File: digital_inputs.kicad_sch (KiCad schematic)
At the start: 37 parts, among them U301 74HC595, U302 74HCT244

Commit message: completed schematic
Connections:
- net +3V3 renamed +3.3V

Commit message: placed components and began routing
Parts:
- RN301: footprint (none) -> Resistor_SMD:R_Array_Convex_8x0602
- U302: footprint Package_SO:SOIC-16_3.9x9.9mm_P1.27mm -> Package_SO:SOIC-20W_7.5x12.8mm_P1.27mm
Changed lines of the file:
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@@
       (effects (font (size 1.27 1.27)) (justify left))
     )
-    (property "Footprint" "Package_SO:SOIC-16_3.9x9.9mm_P1.27mm" (at 234.95 110.49 0)
+    (property "Footprint" "Package_SO:SOIC-20W_7.5x12.8mm_P1.27mm" (at 234.95 110.49 0)
       (effects (font (size 1.27 1.27)) hide)
     )
@@
       (effects (font (size 1.27 1.27)))
     )
-    (property "Footprint" "" (at 252.73 59.055 90)
-      (effects (font (size 1.27 1.27)) hide)
-    )
+    (property "Footprint" "Resistor_SMD:R_Array_Convex_8x0602" (at 252.73 59.055 90)
+      (effects (font (size 1.27 1.27)) hide)
+    )

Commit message: majority of layout done
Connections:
- net D_In_0_pullup: now also RN301.9 (R8.2); no longer RN301.16 (R1.2)
- net D_In_1_pullup: now also RN301.10 (R7.2); no longer RN301.15 (R2.2)
- net D_In_2_pullup: now also RN301.11 (R6.2); no longer RN301.14 (R3.2)
- net D_In_3_pullup: now also RN301.12 (R5.2); no longer RN301.13 (R4.2)
- net D_In_4_pullup: now also RN301.13 (R4.2); no longer RN301.12 (R5.2)
- net D_In_5_pullup: now also RN301.14 (R3.2); no longer RN301.11 (R6.2)
- net D_In_6_pullup: now also RN301.15 (R2.2); no longer RN301.10 (R7.2)
- net D_In_7_pullup: now also RN301.16 (R1.2); no longer RN301.9 (R8.2)
- net at RN301.1 (R1.1): now also U301.7 (QH); no longer U301.15 (QA)
- net at RN301.2 (R2.1): now also U301.6 (QG); no longer U301.1 (QB)
- net at RN301.3 (R3.1): now also U301.5 (QF); no longer U301.2 (QC)
- net at RN301.4 (R4.1): now also U301.4 (QE); no longer U301.3 (QD)
- net at RN301.5 (R5.1): now also U301.3 (QD); no longer U301.4 (QE)
- net at RN301.6 (R6.1): now also U301.2 (QC); no longer U301.5 (QF)
- net at RN301.7 (R7.1): now also U301.1 (QB); no longer U301.6 (QG)
- net at RN301.8 (R8.1): now also U301.15 (QA); no longer U301.7 (QH)
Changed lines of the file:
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@@
     )
   )
-  (symbol (lib_id "Device:R_Pack08") (at 252.73 46.99 270) (unit 1)
-    (in_bom yes) (on_board yes) (dnp no) (fields_autoplaced)
-    (property "Reference" "RN301" (at 252.73 30.48 90)
+  (symbol (lib_id "Device:R_Pack08") (at 252.73 44.45 270) (mirror x) (unit 1)
+    (in_bom yes) (on_board yes) (dnp no)
+    (property "Reference" "RN301" (at 252.73 60.96 90)
       (effects (font (size 1.27 1.27)))
     )
-    (property "Value" "10k" (at 252.73 33.02 90)
+    (property "Value" "10k" (at 252.73 58.42 90)
       (effects (font (size 1.27 1.27)))
     )
-    (property "Footprint" "Resistor_SMD:R_Array_Convex_8x0602" (at 252.73 59.055 90)
+    (property "Footprint" "Resistor_SMD:R_Array_Convex_8x0602" (at 252.73 32.385 90)
       (effects (font (size 1.27 1.27)) hide)
     )
-    (property "Datasheet" "~" (at 252.73 46.99 0)
+    (property "Datasheet" "~" (at 252.73 44.45 0)
       (effects (font (size 1.27 1.27)) hide)
     )

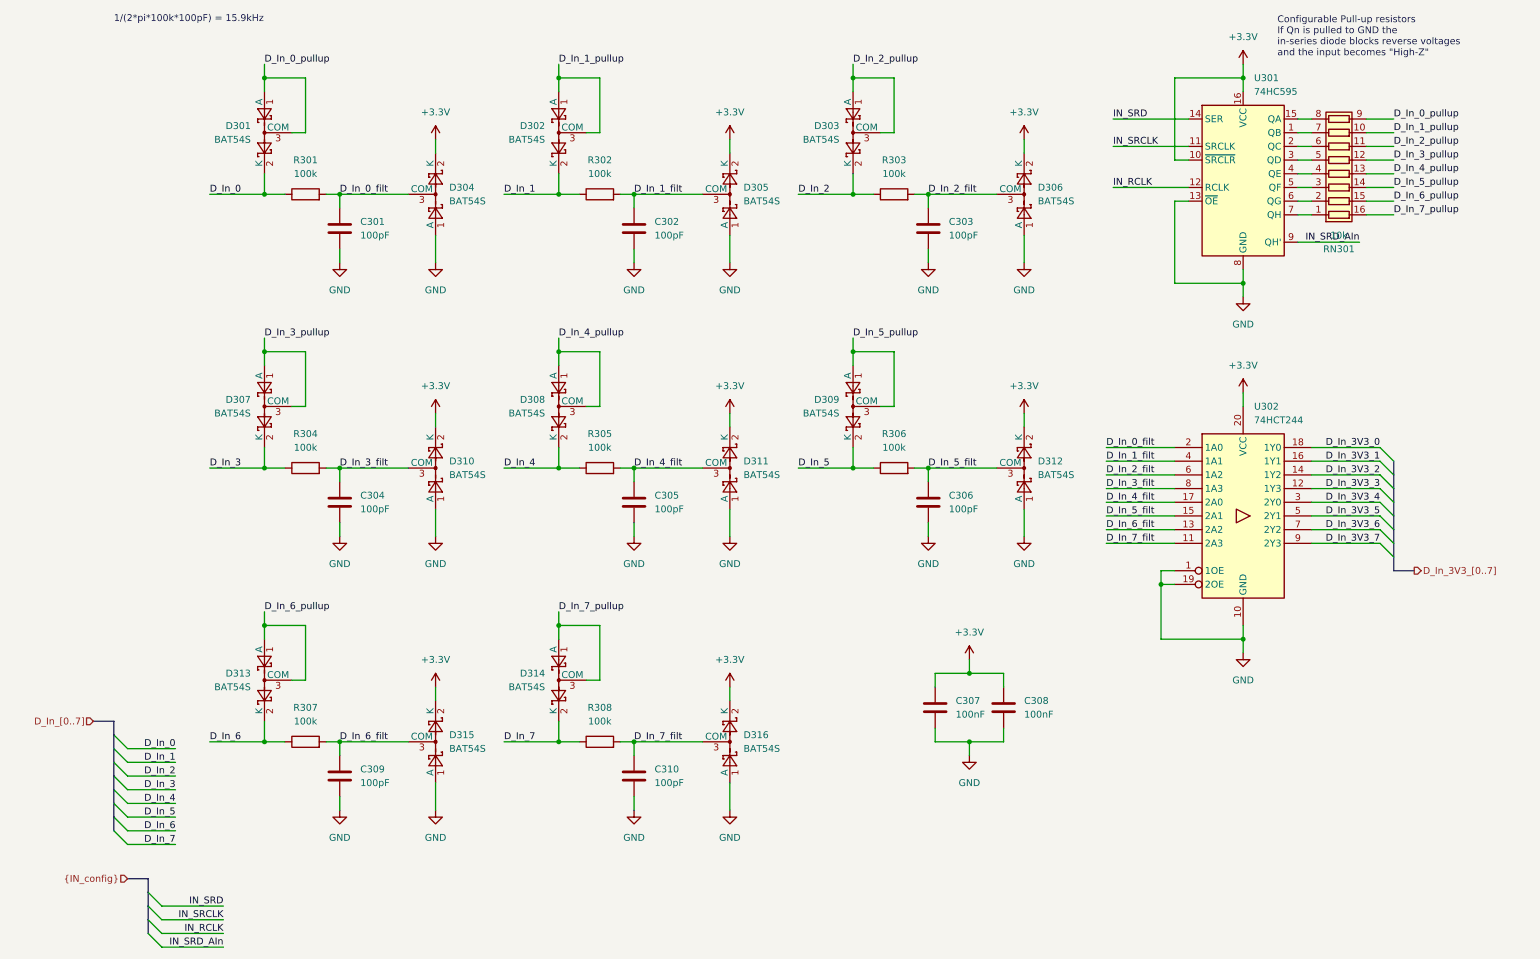
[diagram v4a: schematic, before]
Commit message: hierarchical sheets for digital I/O and replaced power supply jumpers with relays
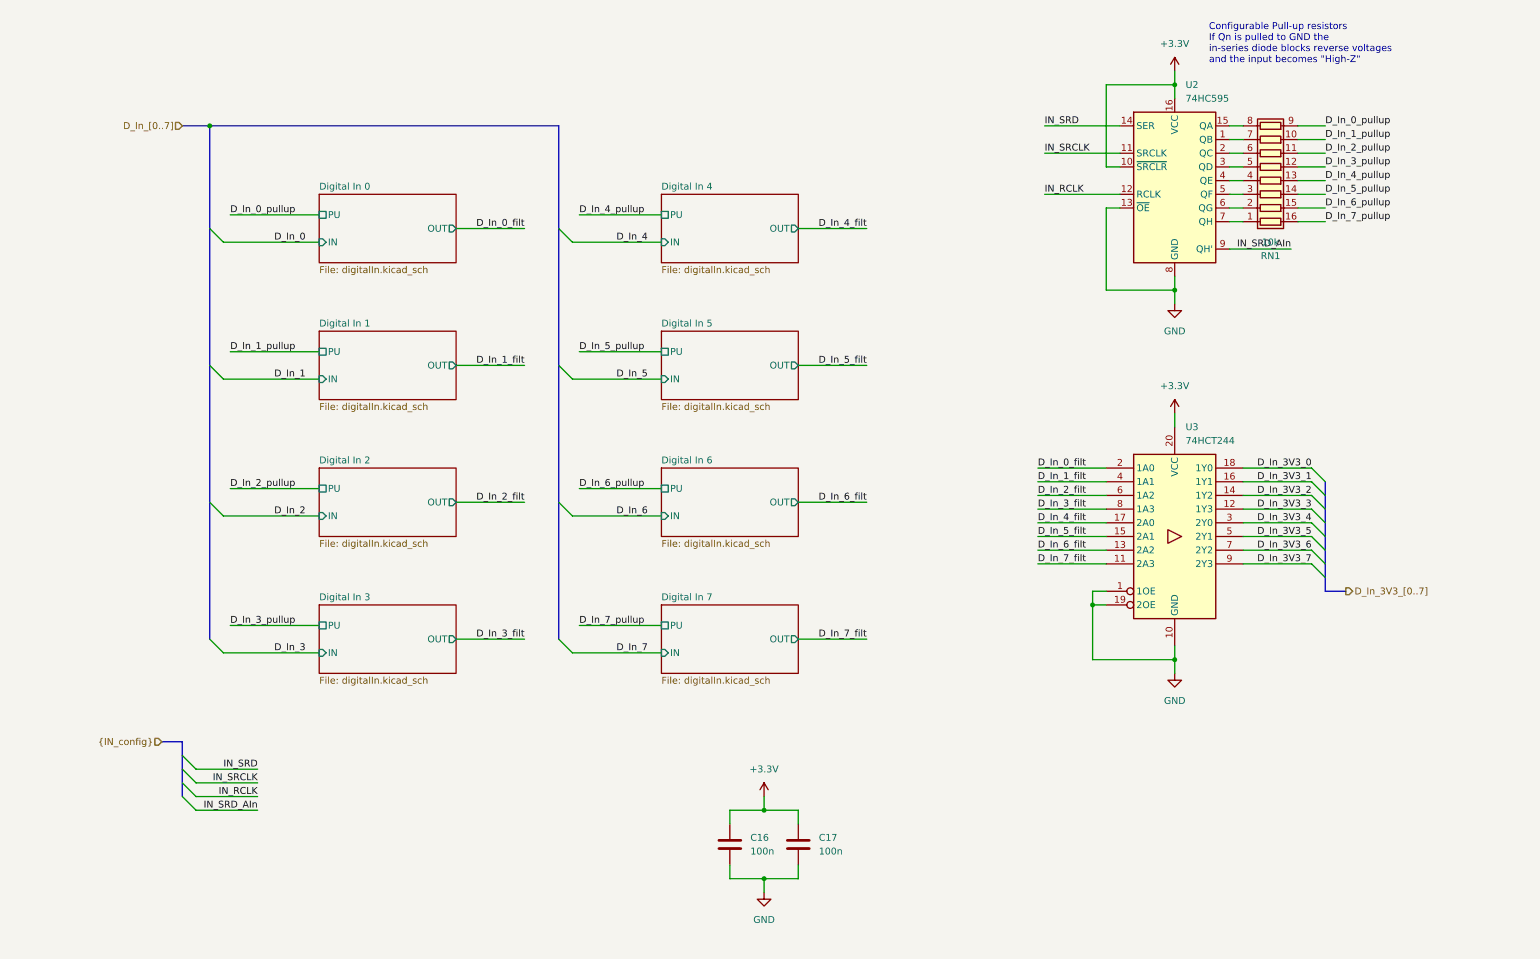
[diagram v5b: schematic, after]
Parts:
- removed C301, C302, C303, C304, C305, C306, C309, C310: 100pF, Capacitor_SMD:C_0603_1608Metric, symbol Device:C
- removed D301, D302, D303, D304, D305, D306, D307, D308, D309, D310, D311, D312, D313, D314, D315, D316: BAT54S, Package_TO_SOT_SMD:SOT-23, symbol Diode:BAT54S
- removed R301, R302, R303, R304, R305, R306, R307, R308: 100k, Resistor_SMD:R_0603_1608Metric, symbol Device:R
- C16: renamed from C307; value 100nF -> 100n
- C17: renamed from C308; value 100nF -> 100n
- renumbered RN301 to RN1, U301 to U2, U302 to U3
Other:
- added sheet Digital In 0 (digitalIn.kicad_sch)
- added sheet Digital In 1 (digitalIn.kicad_sch)
- added sheet Digital In 2 (digitalIn.kicad_sch)
- added sheet Digital In 3 (digitalIn.kicad_sch)
- added sheet Digital In 4 (digitalIn.kicad_sch)
- added sheet Digital In 5 (digitalIn.kicad_sch)
- added sheet Digital In 6 (digitalIn.kicad_sch)
- added sheet Digital In 7 (digitalIn.kicad_sch)
- note removed: "1/(2*pi*100k*100pF) = 15.9kHz"
- moved on the sheet: C16, C17, RN1, U2, U3

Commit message: added missing values and possible improvements
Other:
- note added: "wenn IOs verbunden: kein Pullup notwendig bzw. bereits durch output Stufe verfügbar"
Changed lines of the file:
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@@
     (stroke (width 0) (type default))
+  )
+  (text "wenn IOs verbunden: kein Pullup notwendig\nbzw. bereits durch output Stufe verfügbar"
+    (at 231.14 71.12 0)
+    (effects (font (size 1.27 1.27)) (justify left bottom))
   )
   (text "Configurable Pull-up resistors\nIf Qn is pulled to GND the\nin-series diode blocks reverse voltages\nand the input becomes \"High-Z\""
